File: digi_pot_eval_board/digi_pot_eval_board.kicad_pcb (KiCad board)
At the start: 2 copper layers, 101.6 x 162.6 mm, 77 parts, among them J1 Conn_01x07_Male, J2 Conn_01x10_Male, J3 47346-0001, J4 DS-210, J5 DIN-5-OOTDTY, J6 DIN-5-OOTDTY, J7 JST-04, J8 DS1013-06S, K2 G6K2FYTR5DC, K4 G6K2FYTR5DC, K5 G6K2FYTR5DC, K6 G6K2FYTR5DC, K7 G6K2FYTR5DC, Q1 BSS84, Q2 BSS84, SW3 SW_Push, U1 DigiPot, U10 6N138, U11 NCP1117ST50T3G, U12 ATmega32U4-AU, U2 DigiPot, U3 DigiPot, U4 DigiPot, U5 DigiPot, U6 DigiPot, U7 DigiPot, U8 ULN2003A, U9 USBLC6-2SC6, Y1 16MHz HC-49SM

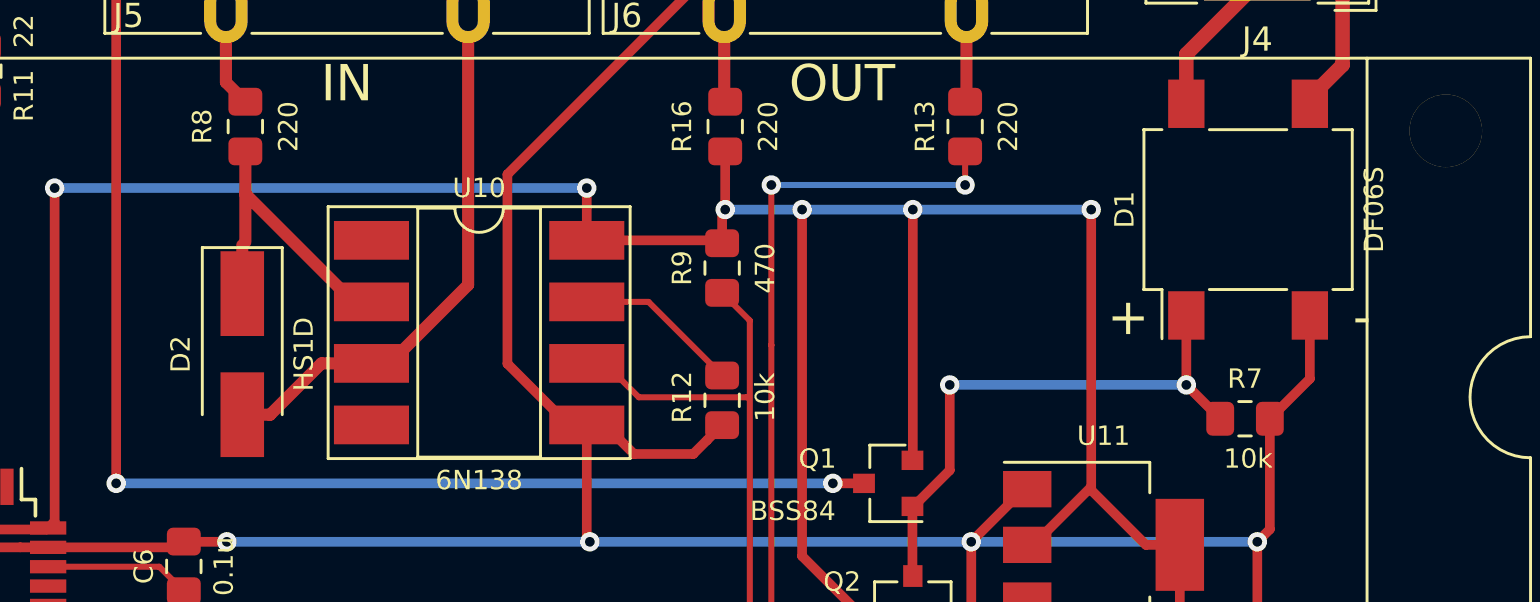
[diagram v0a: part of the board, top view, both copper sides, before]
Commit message: Fixing MIDI optocoupler protection diode footprint.
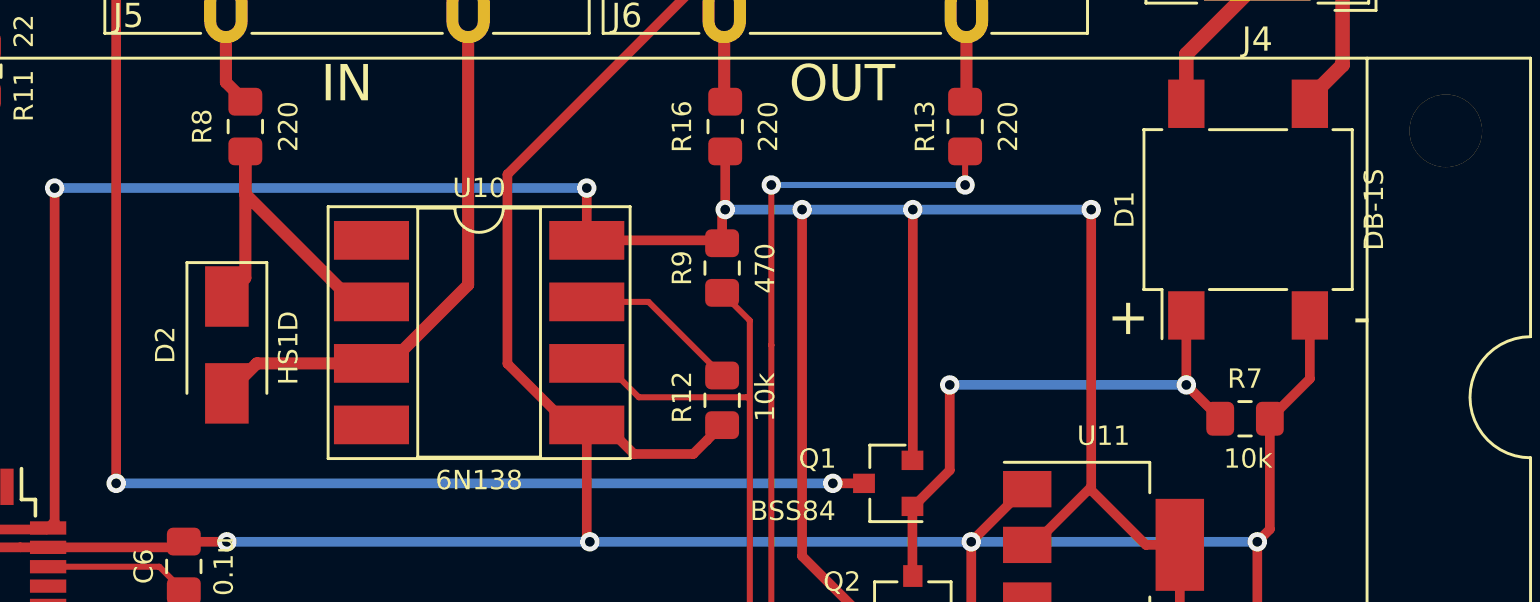
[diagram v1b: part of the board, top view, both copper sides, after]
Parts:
- D1: value DF06S -> DB-1S
- D2: footprint Diode_SMD:D_SMA_Handsoldering -> Diode_SMD:D_SMA
- moved D2 0.74 mm to (110.9, 58.0)
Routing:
- net Net-(D2-Pad1): track 13.0 -> 15.1 mm
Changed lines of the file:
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@@
   (general
     (thickness 1.6)
-    (drawings 46)
-    (tracks 1121)
+    (drawings 48)
+    (tracks 1118)
     (zones 0)
     (modules 77)
@@
   )
   (page A4)
+  (title_block
+    (title "DigiPot Evaluation Board")
+    (date 2019-10-14)
+    (rev 0.3)
+  )
   (layers
     (0 F.Cu signal)
@@
     (add_net VBUS)
   )
+  (module Diode_SMD:D_SMA (layer F.Cu)
+    (at 110.871 58.039 270)
+    (descr "Diode SMA (DO-214AC)")
+    (tags "Diode SMA (DO-214AC)")
+    (attr smd)
+    (fp_text reference D2 (at 0 2.54 270) (layer F.SilkS)
+      (effects (font (size 0.8 0.8) (thickness 0.15)))
+    )
+    (fp_text value HS1D (at 0.127 -2.54 270) (layer F.SilkS)
+      (effects (font (size 0.8 0.8) (thickness 0.1)))
+    )
+    (fp_line (start -3.4 -1.65) (end 2 -1.65) (layer F.SilkS) (width 0.12))
+    (fp_line (start -3.4 1.65) (end 2 1.65) (layer F.SilkS) (width 0.12))
+    (fp_line (start -0.64944 0.00102) (end 0.50118 -0.79908) (layer F.Fab) (width 0.1))
+    (fp_line (start -0.64944 0.00102) (end 0.50118 0.75032) (layer F.Fab) (width 0.1))
+    (fp_line (start 0.50118 0.75032) (end 0.50118 -0.79908) (layer F.Fab) (width 0.1))
+    (fp_line (start -0.64944 -0.79908) (end -0.64944 0.80112) (layer F.Fab) (width 0.1))
+    (fp_line (start 0.50118 0.00102) (end 1.4994 0.00102) (layer F.Fab) (width 0.1))
+    (fp_line (start -0.64944 0.00102) (end -1.55114 0.00102) (layer F.Fab) (width 0.1))
+    (fp_line (start -3.5 1.75) (end -3.5 -1.75) (layer F.CrtYd) (width 0.05))
+    (fp_line (start 3.5 1.75) (end -3.5 1.75) (layer F.CrtYd) (width 0.05))
+    (fp_line (start 3.5 -1.75) (end 3.5 1.75) (layer F.CrtYd) (width 0.05))
+    (fp_line (start -3.5 -1.75) (end 3.5 -1.75) (layer F.CrtYd) (width 0.05))
+    (fp_line (start 2.3 -1.5) (end -2.3 -1.5) (layer F.Fab) (width 0.1))
+    (fp_line (start 2.3 -1.5) (end 2.3 1.5) (layer F.Fab) (width 0.1))
+    (fp_line (start -2.3 1.5) (end -2.3 -1.5) (layer F.Fab) (width 0.1))
+    (fp_line (start 2.3 1.5) (end -2.3 1.5) (layer F.Fab) (width 0.1))
+    (fp_line (start -3.4 -1.65) (end -3.4 1.65) (layer F.SilkS) (width 0.12))
+    (fp_text user %R (at -2.54 -2.54 270) (layer F.Fab)
+      (effects (font (size 1 1) (thickness 0.15)))
+    )
+    (pad 2 smd rect (at 2 0 270) (size 2.5 1.8) (layers F.Cu F.Paste F.Mask)
+      (net 89 "Net-(D2-Pad2)"))
+    (pad 1 smd rect (at -2 0 270) (size 2.5 1.8) (layers F.Cu F.Paste F.Mask)
+      (net 94 "Net-(D2-Pad1)"))
+    (model ${KISYS3DMOD}/Diode_SMD.3dshapes/D_SMA.wrl
+      (at (xyz 0 0 0))
+      (scale (xyz 1 1 1))
+      (rotate (xyz 0 0 0))
+    )
+  )
   (module Crystal:Crystal_SMD_HC49-SD (layer F.Cu)
     (at 82.931 69.215 90)
@@
     (pad 1 np_thru_hole circle (at 0 0) (size 3.2 3.2) (drill 3.2) (layers *.Cu *.Mask))
   )
-  (module Diode_SMD:D_SMA_Handsoldering (layer F.Cu)
-    (at 111.506 58.42 270)
-    (descr "Diode SMA (DO-214AC) Handsoldering")
-    (tags "Diode SMA (DO-214AC) Handsoldering")
-    (attr smd)
-    (fp_text reference D2 (at 0 2.54 270) (layer F.SilkS)
-      (effects (font (size 0.8 0.8) (thickness 0.15)))
-    )
-    (fp_text value HS1D (at 0 -2.54 270) (layer F.SilkS)
-      (effects (font (size 0.8 0.8) (thickness 0.1)))
-    )
-    (fp_line (start -4.4 -1.65) (end 2.5 -1.65) (layer F.SilkS) (width 0.12))
-    (fp_line (start -4.4 1.65) (end 2.5 1.65) (layer F.SilkS) (width 0.12))
-    (fp_line (start -0.64944 0.00102) (end 0.50118 -0.79908) (layer F.Fab) (width 0.1))
-    (fp_line (start -0.64944 0.00102) (end 0.50118 0.75032) (layer F.Fab) (width 0.1))
-    (fp_line (start 0.50118 0.75032) (end 0.50118 -0.79908) (layer F.Fab) (width 0.1))
-    (fp_line (start -0.64944 -0.79908) (end -0.64944 0.80112) (layer F.Fab) (width 0.1))
-    (fp_line (start 0.50118 0.00102) (end 1.4994 0.00102) (layer F.Fab) (width 0.1))
-    (fp_line (start -0.64944 0.00102) (end -1.55114 0.00102) (layer F.Fab) (width 0.1))
-    (fp_line (start -4.5 1.75) (end -4.5 -1.75) (layer F.CrtYd) (width 0.05))
-    (fp_line (start 4.5 1.75) (end -4.5 1.75) (layer F.CrtYd) (width 0.05))
-    (fp_line (start 4.5 -1.75) (end 4.5 1.75) (layer F.CrtYd) (width 0.05))
-    (fp_line (start -4.5 -1.75) (end 4.5 -1.75) (layer F.CrtYd) (width 0.05))
-    (fp_line (start 2.3 -1.5) (end -2.3 -1.5) (layer F.Fab) (width 0.1))
-    (fp_line (start 2.3 -1.5) (end 2.3 1.5) (layer F.Fab) (width 0.1))
-    (fp_line (start -2.3 1.5) (end -2.3 -1.5) (layer F.Fab) (width 0.1))
-    (fp_line (start 2.3 1.5) (end -2.3 1.5) (layer F.Fab) (width 0.1))
-    (fp_line (start -4.4 -1.65) (end -4.4 1.65) (layer F.SilkS) (width 0.12))
-    (fp_text user %R (at 2.921 -2.54 270) (layer F.Fab)
-      (effects (font (size 1 1) (thickness 0.15)))
-    )
-    (pad 2 smd rect (at 2.5 0 270) (size 3.5 1.8) (layers F.Cu F.Paste F.Mask)
-      (net 89 "Net-(D2-Pad2)"))
-    (pad 1 smd rect (at -2.5 0 270) (size 3.5 1.8) (layers F.Cu F.Paste F.Mask)
-      (net 94 "Net-(D2-Pad1)"))
-    (model ${KISYS3DMOD}/Diode_SMD.3dshapes/D_SMA.wrl
-      (at (xyz 0 0 0))
-      (scale (xyz 1 1 1))
-      (rotate (xyz 0 0 0))
-    )
-  )
   (module Capacitor_THT:CP_Radial_D4.0mm_P2.00mm (layer F.Cu)
     (at 113.03 175.768 180)
@@
       (effects (font (size 0.8 0.8) (thickness 0.15)))
     )
-    (fp_text value DF06S (at 0 5.2 90) (layer F.SilkS)
+    (fp_text value DB-1S (at 0 5.2 90) (layer F.SilkS)
       (effects (font (size 0.8 0.8) (thickness 0.1)))
     )
@@
     (pad 1 np_thru_hole circle (at 0 0) (size 3.2 3.2) (drill 3.2) (layers *.Cu *.Mask))
   )
+  (dimension 162.56 (width 0.3) (layer F.SilkS)
+    (gr_text "162.560 mm" (at 176.344 110.49 270) (layer F.SilkS)
+      (effects (font (size 1.5 1.5) (thickness 0.3)))
+    )
+    (feature1 (pts (xy 161.798 191.77) (xy 174.830421 191.77)))
+    (feature2 (pts (xy 161.798 29.21) (xy 174.830421 29.21)))
+    (crossbar (pts (xy 174.244 29.21) (xy 174.244 191.77)))
+    (arrow1a (pts (xy 174.244 191.77) (xy 173.657579 190.643496)))
+    (arrow1b (pts (xy 174.244 191.77) (xy 174.830421 190.643496)))
+    (arrow2a (pts (xy 174.244 29.21) (xy 173.657579 30.336504)))
+    (arrow2b (pts (xy 174.244 29.21) (xy 174.830421 30.336504)))
+  )
+  (dimension 101.600079 (width 0.3) (layer F.SilkS)
+    (gr_text "101.600 mm" (at 115.598339 18.032551 359.9283803) (layer F.SilkS)
+      (effects (font (size 1.5 1.5) (thickness 0.3)))
+    )
+    (feature1 (pts (xy 166.37 40.767) (xy 166.396447 19.609629)))
+    (feature2 (pts (xy 64.77 40.64) (xy 64.796447 19.482629)))
+    (crossbar (pts (xy 64.795714 20.069049) (xy 166.395714 20.196049)))
+    (arrow1a (pts (xy 166.395714 20.196049) (xy 165.268478 20.781061)))
+    (arrow1b (pts (xy 166.395714 20.196049) (xy 165.269944 19.608221)))
+    (arrow2a (pts (xy 64.795714 20.069049) (xy 65.921484 20.656877)))
+    (arrow2b (pts (xy 64.795714 20.069049) (xy 65.92295 19.484037)))
+  )
   (gr_text LW (at 99.06 97.536 270) (layer B.SilkS)
     (effects (font (size 0.7 0.7) (thickness 0.1)) (justify right mirror))
@@
   (segment (start 83.634 64.965) (end 87.465 68.796) (width 0.5) (layer F.Cu) (net 77))
   (segment (start 82.931 64.965) (end 83.634 64.965) (width 0.5) (layer F.Cu) (net 77))
-  (segment (start 82.872 65.024) (end 82.931 64.965) (width 0.5) (layer F.Cu) (net 77) (status 1000000))
-  (segment (start 78.495 65.024) (end 82.872 65.024) (width 0.5) (layer F.Cu) (net 77) (status 1000000))
+  (segment (start 82.872 65.024) (end 82.931 64.965) (width 0.5) (layer F.Cu) (net 77))
+  (segment (start 78.495 65.024) (end 82.872 65.024) (width 0.5) (layer F.Cu) (net 77))
   (segment (start 108.081 67.196) (end 109.093 68.208) (width 0.25) (layer F.Cu) (net 78))
   (segment (start 103.49 67.196) (end 108.081 67.196) (width 0.25) (layer F.Cu) (net 78))
@@
   (segment (start 120.831 55.56) (end 117.59 58.801) (width 0.5) (layer F.Cu) (net 89))
   (segment (start 120.831 44.283) (end 120.831 55.56) (width 0.5) (layer F.Cu) (net 89))
-  (segment (start 115.04 58.801) (end 116.84 58.801) (width 0.5) (layer F.Cu) (net 89))
-  (segment (start 114.775 58.801) (end 115.04 58.801) (width 0.5) (layer F.Cu) (net 89))
-  (segment (start 112.656 60.92) (end 114.775 58.801) (width 0.5) (layer F.Cu) (net 89))
-  (segment (start 111.506 60.92) (end 112.656 60.92) (width 0.5) (layer F.Cu) (net 89))
+  (segment (start 112.109 58.801) (end 110.871 60.039) (width 0.5) (layer F.Cu) (net 89))
+  (segment (start 116.84 58.801) (end 112.109 58.801) (width 0.5) (layer F.Cu) (net 89))
   (segment (start 141.405 47.943) (end 141.351 47.997) (width 0.25) (layer F.Cu) (net 90))
   (segment (start 141.405 44.283) (end 141.405 47.943) (width 0.5) (layer F.Cu) (net 90))
@@
   (segment (start 116.09 56.261) (end 116.84 56.261) (width 0.25) (layer F.Cu) (net 94))
   (segment (start 111.633 50.047) (end 111.633 51.804) (width 0.5) (layer F.Cu) (net 94))
-  (segment (start 111.633 53.793) (end 111.633 51.804) (width 0.5) (layer F.Cu) (net 94))
-  (segment (start 111.506 53.92) (end 111.633 53.793) (width 0.25) (layer F.Cu) (net 94))
-  (segment (start 111.506 55.92) (end 111.506 53.92) (width 0.5) (layer F.Cu) (net 94))
+  (segment (start 111.633 55.277) (end 110.871 56.039) (width 0.5) (layer F.Cu) (net 94) (status 1000000))
+  (segment (start 111.633 50.047) (end 111.633 55.277) (width 0.5) (layer F.Cu) (net 94) (status 1000000))
   (via (at 95.25 72.009) (size 0.8) (drill 0.4) (layers F.Cu B.Cu) (net 95))
   (segment (start 95.237 71.996) (end 95.25 72.009) (width 0.25) (layer F.Cu) (net 95))

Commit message: Before wide nav_panel and Level pot move.
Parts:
- added J10: AudioJack3, Connectors:phone-jack-6.3, B.Cu at (80.0, 40.6)
- added J11: Conn_01x02_Male, Connector_JST:JST_EH_B02B-EH-A_1x02_P2.50mm_Vertical, B.Cu at (116.8, 48.9)
- added J12: Conn_01x03_Male, Connector_JST:JST_EH_B03B-EH-A_1x03_P2.50mm_Vertical, B.Cu at (139.1, 48.9)
- added J13: Conn_01x06_Male, Connector_JST:JST_EH_B06B-EH-A_1x06_P2.50mm_Vertical, F.Cu at (78.7, 94.0)
- added J9: AudioJack3, Connectors:phone-jack-6.3, B.Cu at (94.0, 40.6)
- moved J5 16.9 mm to (109.5, 24.9)
- moved J6 16.9 mm to (130.0, 24.9)
- moved R10 12.4 mm to (98.6, 59.2)
- moved R11 12.4 mm to (101.1, 59.2)
- moved REF** 8.79 mm to (116.3, 51.4)
- moved PAN1 7.62 mm to (116.8, 76.2)
- moved R8 4.91 mm to (113.4, 53.6)
- moved U9 4.70 mm to (99.8, 46.5)
- moved R16 4.50 mm to (132.7, 53.3)
- moved R13 4.33 mm to (141.6, 53.3)
- moved D2 3.86 mm to (113.7, 60.7)
- moved R9 3.82 mm to (132.7, 58.4)
- moved U10 3.70 mm to (123.2, 60.7)
- moved R12 3.47 mm to (132.7, 63.5)
- moved C7 3.30 mm to (94.0, 57.3), turned to 90 degrees
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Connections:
- net Net-(D2-Pad2) renamed MIN5
- net Net-(J5-Pad4) renamed MIN4
- net Net-(J6-Pad4) renamed MOUT4
- net Net-(J6-Pad5) renamed MOUT5
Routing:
- net +5V: track 641.5 -> 495.4 mm, vias 26 -> 20
- net GND: track 735.9 -> 604.9 mm, vias 32 -> 25
- net VBUS: track 86.3 -> 0.00 mm, vias 2 -> 0
- net TX: track 72.0 -> 0.00 mm, vias 4 -> 0
- net RX: track 63.9 -> 0.00 mm, vias 2 -> 0
- net MIN5: track 23.1 -> 0.00 mm
- net D-: track 16.4 -> 0.00 mm
- net D+: track 16.4 -> 0.00 mm
- net Net-(D2-Pad1): track 15.1 -> 0.00 mm
- net Net-(D1-Pad3): track 13.6 -> 0.00 mm
- net Net-(J3-Pad2): track 7.63 -> 0.00 mm
- net Net-(J3-Pad3): track 7.58 -> 0.00 mm
- net Net-(C7-Pad1): track 7.38 -> 0.00 mm
- net Net-(R12-Pad1): track 6.85 -> 0.00 mm
- net RE_A: track 31.9 -> 25.1 mm
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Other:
- board size 101.6 x 162.6 mm -> 103.6 x 162.6 mm

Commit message: Introducing new layout.
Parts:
- removed J11: Conn_01x02_Male, Connector_JST:JST_EH_B02B-EH-A_1x02_P2.50mm_Vertical
- removed J12: Conn_01x03_Male, Connector_JST:JST_EH_B03B-EH-A_1x03_P2.50mm_Vertical
- removed J4: DS-210, Connector_BarrelJack:BarrelJack_Wuerth_6941xx301002
- removed J5, J6: DIN-5-OOTDTY, Connectors:DIN5MIDI-OOTDTY
- removed J7: JST-04, Connector_JST:JST_EH_B04B-EH-A_1x04_P2.50mm_Vertical
- removed the REF** at (163.4, 34.2)
- removed the REF** at (116.3, 51.4)
- removed the REF** at (68.8, 35.2)
- added REF**: DIN-5-OOTDTY, Connectors:DIN5MIDI-OOTDTY, F.Cu at (131.4, 41.3)
- added REF**: DISPLAY, OLED:oled1602, F.Cu at (115.6, 62.9)
- added REF**: MountingHole_3.2mm_M3_DIN965, MountingHole:MountingHole_3.2mm_M3_DIN965, F.Cu at (164.5, 34.9)
- added REF**: MountingHole_3.2mm_M3_DIN965, MountingHole:MountingHole_3.2mm_M3_DIN965, F.Cu at (66.7, 34.9)
- added REF**: DIN-5-OOTDTY, Connectors:DIN5MIDI-OOTDTY, F.Cu at (111.1, 41.3)
- J10: value AudioJack3 -> Conn_01x02_Male; footprint Connectors:phone-jack-6.3 -> Connector_JST:JST_EH_B02B-EH-A_1x02_P2.50mm_Vertical
- J9: value AudioJack3 -> Conn_01x05_Male; footprint Connectors:phone-jack-6.3 -> Connector_JST:JST_EH_B05B-EH-A_1x05_P2.50mm_Vertical
- PAN1: footprint nav_panel:nav_panel_THT -> nav_panel:nav_panel_SMD
- moved U7 97.6 mm to (71.1, 86.4)
- moved ? 97.6 mm to (68.6, 109.2)
- moved R25 96.8 mm to (78.7, 88.9)
- moved C8 84.1 mm to (80.0, 98.4)
- moved J10 79.9 mm to (159.4, 50.2), turned to 0 degrees
- moved ? 76.2 mm to (162.6, 86.4)
- moved C9 71.9 mm to (144.8, 137.8)
- moved U8 71.1 mm to (118.7, 81.3), turned to 0 degrees
- moved K5 61.7 mm to (146.1, 120.7)
- moved J8 56.8 mm to (76.8, 34.9), turned to 90 degrees
- moved R24 50.2 mm to (103.5, 181.0)
- moved J9 40.5 mm to (133.3, 50.2), turned to 180 degrees
- moved J13 38.1 mm to (77.5, 55.9), turned to 180 degrees
- moved K6 31.4 mm to (146.1, 151.1)
- moved K4 28.2 mm to (115.6, 151.1)
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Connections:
- D1 pad 3: Net-(D1-Pad3) -> POW2
- D1 pad 4: Net-(D1-Pad4) -> POW1
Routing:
- net GND: track 604.9 -> 0.00 mm, vias 25 -> 0
- net +5V: track 495.4 -> 0.00 mm, vias 20 -> 0
- net SCL: track 281.9 -> 0.00 mm, vias 9 -> 0
- net CHG: track 271.6 -> 0.00 mm, vias 6 -> 0
- net SDA: track 263.6 -> 0.00 mm, vias 9 -> 0
- net C: track 220.5 -> 0.00 mm, vias 11 -> 0
- net A3: track 153.0 -> 0.00 mm, vias 6 -> 0
- net HW: track 123.8 -> 0.00 mm, vias 2 -> 0
- net SW_PASSBACK: track 121.1 -> 0.00 mm, vias 2 -> 0
- net MW: track 117.0 -> 0.00 mm, vias 2 -> 0
- net A1: track 111.9 -> 0.00 mm, vias 3 -> 0
- net PW1: track 111.4 -> 0.00 mm, vias 2 -> 0
- net Net-(D3-Pad2): track 99.5 -> 0.00 mm
- net LW: track 97.6 -> 0.00 mm, vias 1 -> 0
- net KBP: track 95.0 -> 0.00 mm
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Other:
- board size 103.6 x 162.6 mm -> 110.5 x 160.7 mm
- board text removed: "SCL"
- board text removed: "SDA"
